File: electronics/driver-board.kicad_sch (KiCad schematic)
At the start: 51 parts, among them J2 Conn_01x05_Socket, J3 S4B-XH-A, J4 Qwiic_RA, J5 Conn_01x06_Female, J6 Conn_01x05_Socket, J7 Conn_01x02, SW1 SW_Push, SW2 SW_Push, SW3 SW_Push, SW4 SW_Push, U1 LMR16006YQ3, U3 ESP32-C6-MINI-1/U, U5 TMC5240-TSSOP38, U7 AS5047D

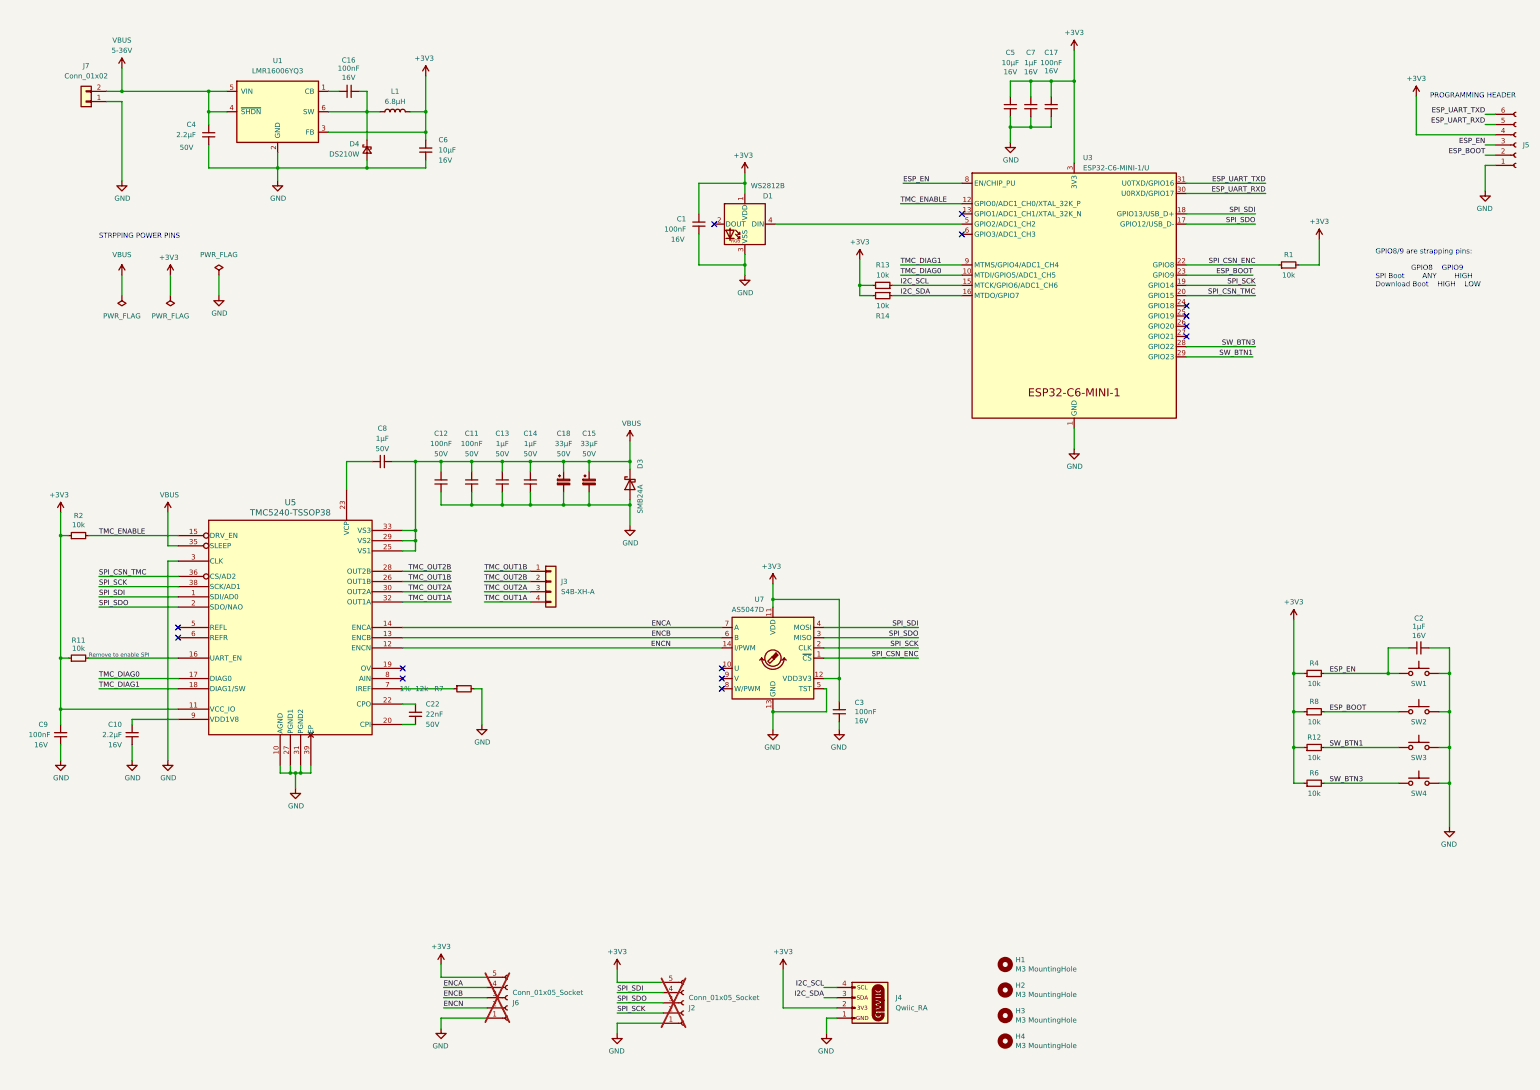
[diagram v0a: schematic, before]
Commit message: changed rgb led and updated routing/tracks
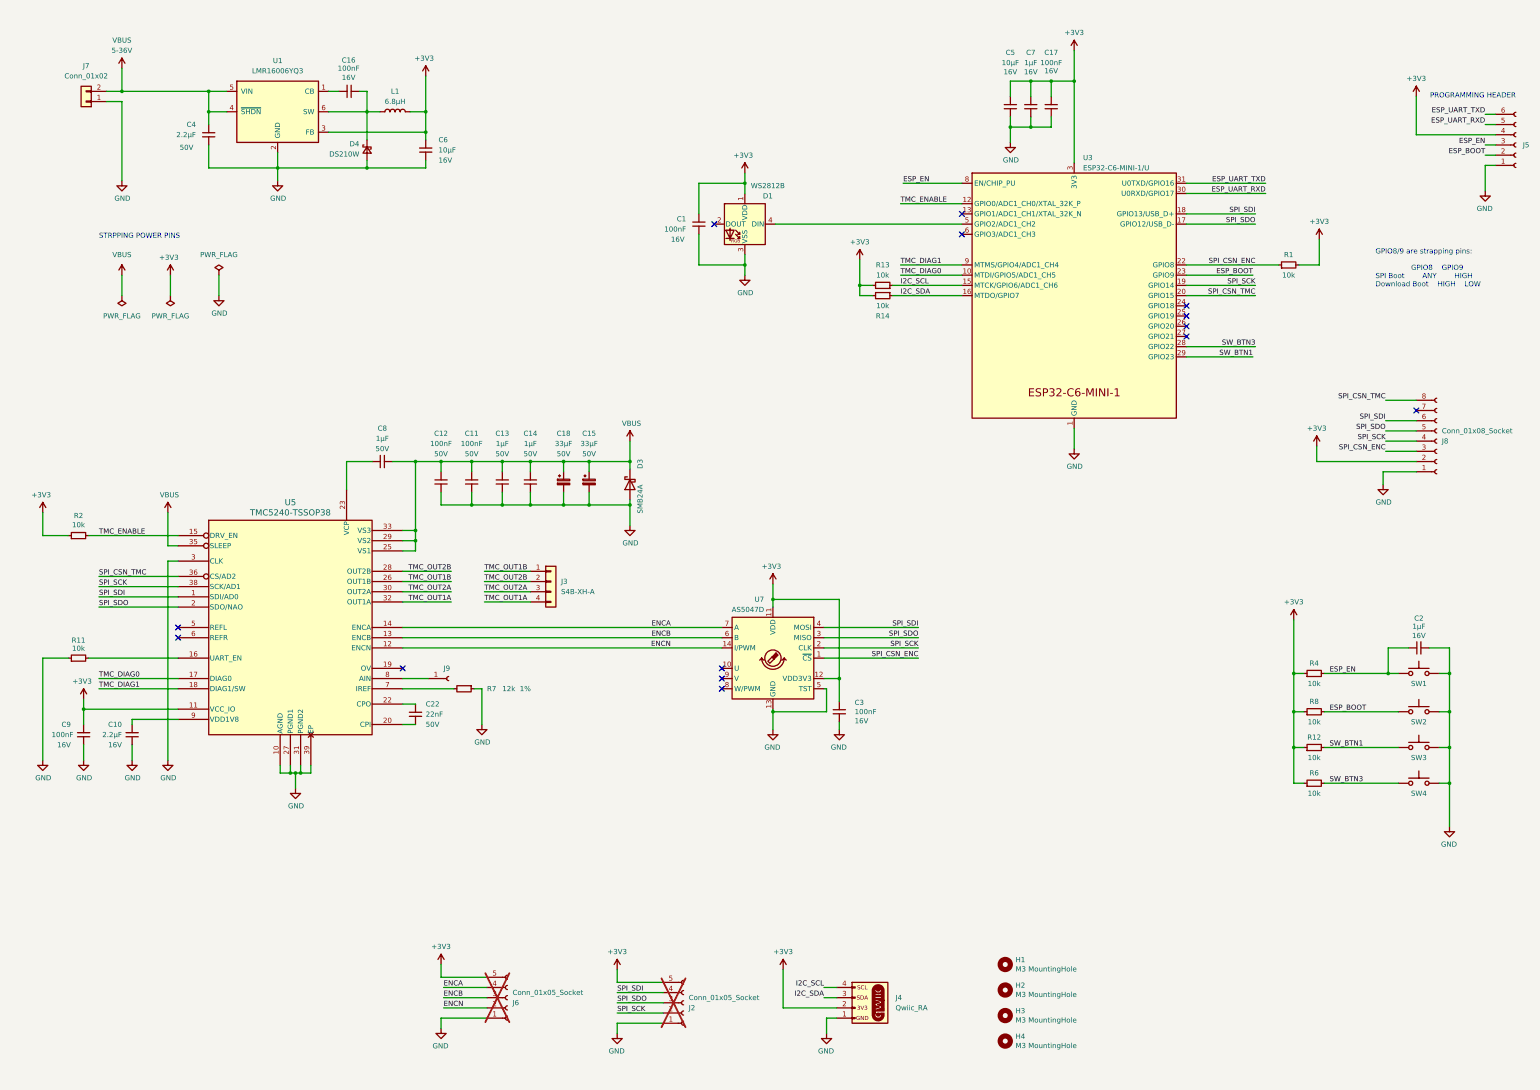
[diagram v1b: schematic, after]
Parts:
- added J8: Conn_01x08_Socket, Connector_PinHeader_2.54mm:PinHeader_2x04_P2.54mm_Vertical, symbol Connector:Conn_01x08_Socket
- added J9: Conn_01x01_Socket, TestPoint:TestPoint_Pad_D2.0mm, symbol Connector:Conn_01x01_Socket
- D1: footprint LED_SMD:LED_WS2812B-2020_PLCC4_2.0x2.0mm -> LED_SMD:LED_SK6812MINI_PLCC4_3.5x3.5mm_P1.75mm; LCSC C965555 -> C527089; Manf# WS2812B-2020 -> WS2812B-Mini
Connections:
- net +3V3: now also J8.2 (Pin_2); no longer R11.1
- net GND: now also R11.1, R7.1, J8.1 (Pin_1); no longer R7.2
- net SPI_CSN_ENC: now also J8.3 (Pin_3)
- net SPI_CSN_TMC: now also J8.8 (Pin_8)
- net SPI_SCK: now also J8.4 (Pin_4)
- net SPI_SDI: now also J8.6 (Pin_6)
- net SPI_SDO: now also J8.5 (Pin_5)
- net at U5.7 (IREF): now also R7.2; no longer R7.1
- net at U5.8 (AIN): now also J9.1 (Pin_1)
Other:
- note removed: "Remove to enable SPI"
- moved on the sheet: C9, R7

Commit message: updates to traces
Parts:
- removed R11: 10k, Resistor_SMD:R_0603_1608Metric, symbol Device:R_Small
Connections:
- no-connect marks 14 -> 15
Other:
- note added: "Internal pull-down enables SPI"
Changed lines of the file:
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@@
   (no_connect (at 312.42 94.615))
   (no_connect (at 194.945 71.755))
+  (no_connect (at 61.595 179.705))
   (no_connect (at 256.54 74.295))
   (no_connect (at 117.475 182.245))
@@
     (stroke (width 0) (type default))
   )
-  (wire (pts (xy 27.94 205.105) (xy 27.94 179.705))
-    (stroke (width 0) (type default))
-  )
-  (wire (pts (xy 39.37 179.705) (xy 61.595 179.705))
-    (stroke (width 0) (type default))
-  )
   (wire (pts (xy 127 130.81) (xy 134.62 130.81))
     (stroke (width 0) (type default))
@@
     (stroke (width 0) (type default))
   )
-  (wire (pts (xy 27.94 179.705) (xy 34.29 179.705))
-    (stroke (width 0) (type default))
-  )
   (wire (pts (xy 226.06 184.785) (xy 226.06 190.5))
     (stroke (width 0) (type default))
@@
   )
   (text "STRPPING POWER PINS" (at 41.91 75.565 0)
+    (effects (font (size 1.27 1.27)) (justify left bottom))
+  )
+  (text "Internal pull-down\nenables SPI\n" (at 78.105 181.61 0)
     (effects (font (size 1.27 1.27)) (justify left bottom))
   )
@@
     )
   )
-  (symbol (lib_id "Device:R_Small") (at 36.83 179.705 90) (unit 1)
-    (in_bom yes) (on_board yes) (dnp no)
-    (property "Reference" "R11" (at 36.83 175.26 90)
-      (effects (font (size 1.27 1.27)))
-    )
-    (property "Value" "10k" (at 36.83 177.292 90)
-      (effects (font (size 1.27 1.27)))
-    )
-    (property "Footprint" "Resistor_SMD:R_0603_1608Metric" (at 36.83 179.705 0)
-      (effects (font (size 1.27 1.27)) hide)
-    )
-    (property "Datasheet" "~" (at 36.83 179.705 0)
-      (effects (font (size 1.27 1.27)) hide)
-    )
-    (property "LCSC" "C4226066" (at 36.83 179.705 90)
-      (effects (font (size 1.27 1.27)) hide)
-    )
-    (property "Manf#" "RT0603FRE1310KL" (at 36.83 179.705 90)
-      (effects (font (size 1.27 1.27)) hide)
-    )
-    (property "Package" "0603" (at 36.83 179.705 90)
-      (effects (font (size 1.27 1.27)) hide)
-    )
-    (pin "1")
-    (pin "2")
-    (instances
-      (project "driver-board"
-        (path "/597a11f2-5d2c-4a65-ac95-38ad106e1367"
-          (reference "R11") (unit 1)
-        )
-      )
-    )
-  )
   (symbol (lib_id "Device:C_Small") (at 127 135.89 0) (unit 1)
     (in_bom yes) (on_board yes) (dnp no)
@@
         )
       )
-    )
-  )
-  (symbol (lib_id "power:GND") (at 27.94 205.105 0) (unit 1)
-    (in_bom yes) (on_board yes) (dnp no)
-    (property "Reference" "#PWR026" (at 27.94 211.455 0)
-      (effects (font (size 1.27 1.27)) hide)
-    )
-    (property "Value" "GND" (at 28.067 209.4992 0)
-      (effects (font (size 1.27 1.27)))
-    )
-    (property "Footprint" "" (at 27.94 205.105 0)
-      (effects (font (size 1.27 1.27)) hide)
-    )
-    (property "Datasheet" "" (at 27.94 205.105 0)
-      (effects (font (size 1.27 1.27)) hide)
-    )
-    (pin "1")
-    (instances
-      (project "driver-board"
-        (path "/597a11f2-5d2c-4a65-ac95-38ad106e1367"
-          (reference "#PWR026") (unit 1)
-        )
-      )
